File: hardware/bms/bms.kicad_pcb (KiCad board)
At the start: 4 copper layers, 120 x 45 mm, 287 parts, among them J1 Screw_Terminal_01x01, J10 Conn_01x10, J11 USB_C_Receptacle_USB2.0, J12 Conn_01x03, J13 Conn_01x07, J2 Screw_Terminal_01x01, J3 Screw_Terminal_01x01, J4 Screw_Terminal_01x01, J5 Screw_Terminal_01x01, J6 Conn_01x02, J7 Conn_01x10, J8 Conn_01x02, J9 Micro_SD_Card_Det2, Q1 MMBT3904, Q2 Q_PMOS_GSD, Q3 Q_PMOS_GSD, Q4 BSZ018N04LS6ATMA1, Q5 IAUC120N04S6N006ATMA1, Q6 IAUC120N04S6N006ATMA1, Q7 BSZ018N04LS6ATMA1, Q8 BSZ018N04LS6ATMA1, Q9 BSZ018N04LS6ATMA1, SW1 SW_SPST, SW2 SW_Push, SW3 SW_Push, U1 BQ76952, U2 LM74700, U3 BQ24610, U4 LM5166X, U5 TPS62172DSG, U6 ESP32-C3-MINI-1-N4, U8 USBLC6-2SC6, U9 TXU0101DCKR

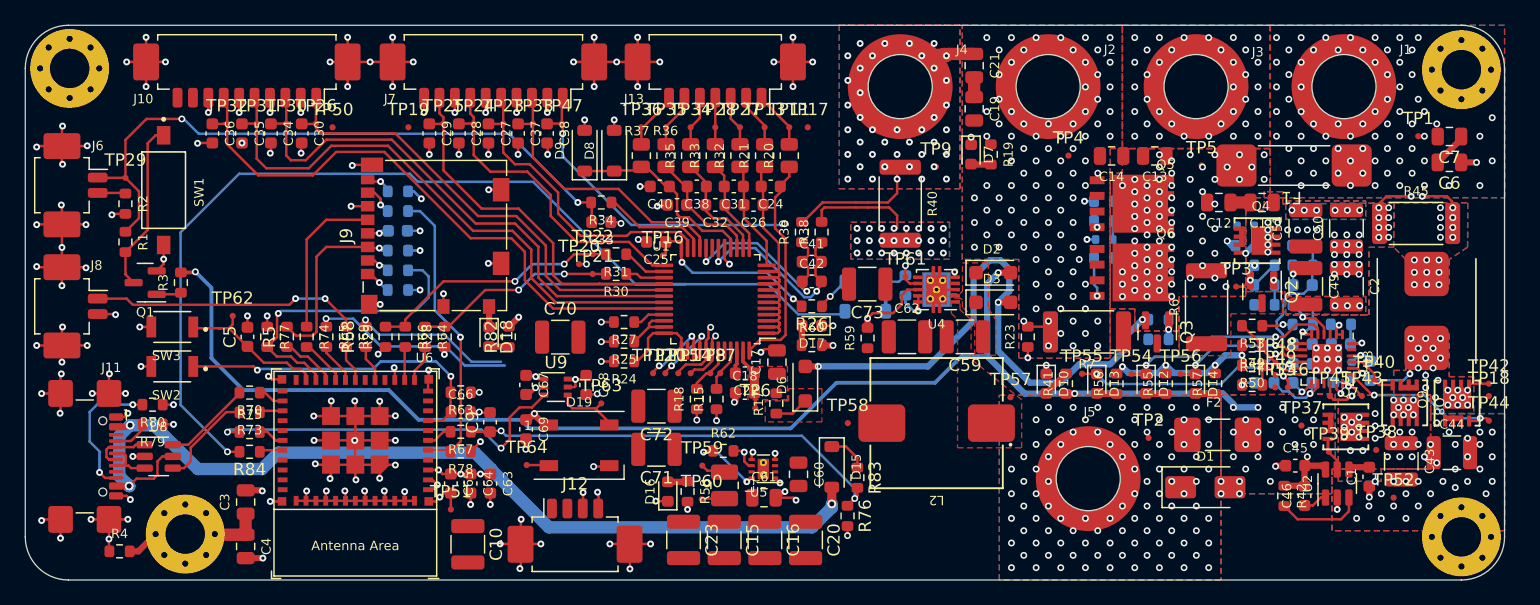
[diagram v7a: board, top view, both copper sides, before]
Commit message: Swapped out SD card holder to a push-push version, should be nicer. Also a lot of routing and power plane work
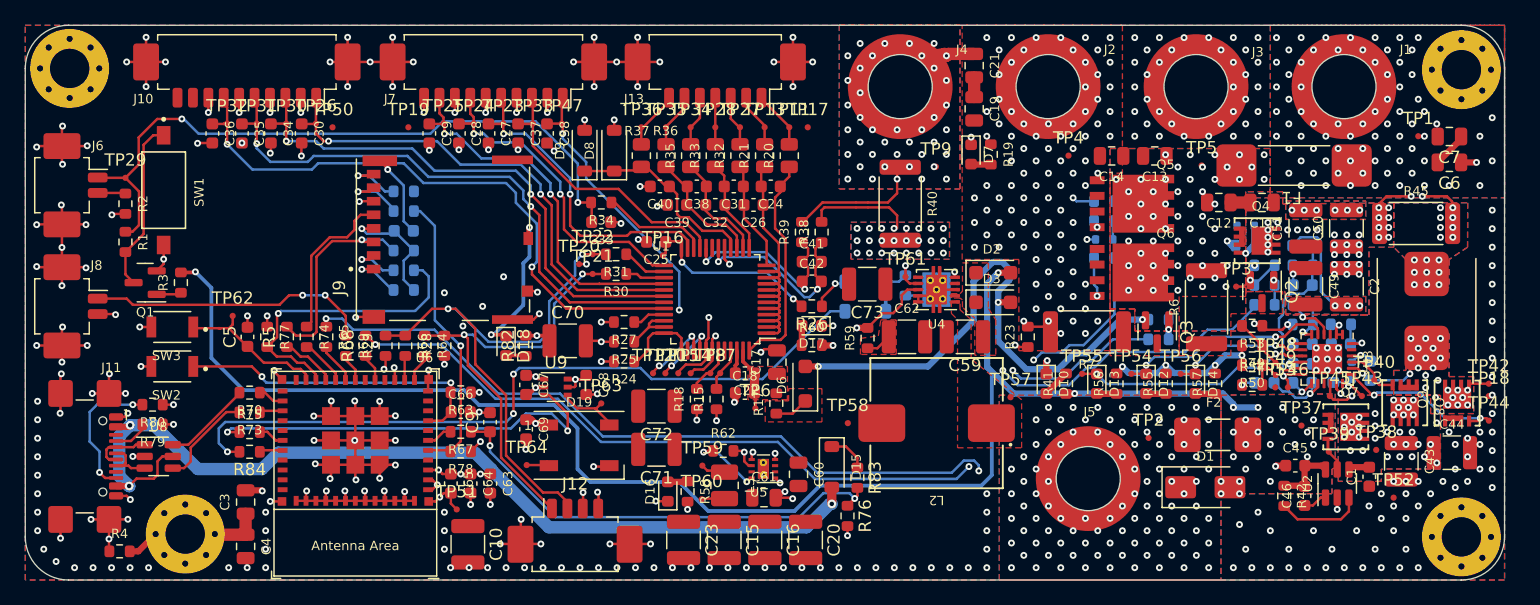
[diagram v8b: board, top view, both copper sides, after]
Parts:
- J9: footprint bms:microSD_HC_Molex_104031-0811 -> bms:MOLEX_503398-1892
- moved D18 1.55 mm to (127.5, 101.0)
- moved R82 1.55 mm to (129.1, 101.0)
- moved J9 0.73 mm to (122.4, 92.4)
- moved R68 0.73 mm to (116.1, 101.0)
- moved R28 0.73 mm to (122.5, 101.0)
- moved R64 0.73 mm to (120.9, 101.0)
- moved R69 0.73 mm to (114.5, 101.0)
- moved R29 0.73 mm to (117.7, 101.0)
- moved R66 0.73 mm to (119.3, 101.0)
- moved C70 0.67 mm to (132.5, 100.6)
- moved C8 0.48 mm to (119.2, 91.7)
- moved R43 0.48 mm to (119.2, 94.9)
- moved R46 0.48 mm to (119.2, 90.1)
- moved R71 0.48 mm to (119.2, 88.5)
- moved R72 0.48 mm to (119.2, 93.3)
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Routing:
- net /BATTERY BALANCE AND MONITOR/DGATE: track 5.58 -> 57.6 mm, vias 1 -> 2
- net /BATTERY BALANCE AND MONITOR/PCHG: track 5.55 -> 56.1 mm, vias 2 -> 3
- net /BATTERY BALANCE AND MONITOR/CGATE: track 22.9 -> 71.4 mm
- net /CHG_STAT1: track 49.3 -> 97.6 mm, vias 3 -> 4
- net /CHG_STAT2: track 42.7 -> 89.7 mm, vias 3 -> 4
- net /BATTERY BALANCE AND MONITOR/PDSG: track 5.68 -> 47.0 mm, vias 2 -> 3
- net /THERM_CHG: track 65.0 -> 100.0 mm
- net /BATTERY BALANCE AND MONITOR/PACK: track 23.0 -> 56.0 mm
- net /MCU/SD_CARD_WRITE: track 92.8 -> 61.0 mm, vias 1 -> 3
- net /BATTERY BALANCE AND MONITOR/I2C_SCL: track 20.6 -> 46.2 mm
- net /BATTERY BALANCE AND MONITOR/I2C_SDA: track 16.4 -> 36.2 mm
- net /BATTERY BALANCE AND MONITOR/LD: track 17.9 -> 33.9 mm
- net /VCHG_IN_F: track 115.6 -> 129.8 mm
- net Net-(D18-K): track 1.67 -> 12.3 mm, vias 0 -> 2
- net GND: track 249.6 -> 255.5 mm, vias 268 -> 354
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- added copper zone on In2.Cu, net /BATTERY CHARGER/SW_NODE
- added copper zone on F.Cu, net Net-(C62-Pad1)
- removed copper zone on B.Cu, net /BATTERY BALANCE AND MONITOR/PACK+
